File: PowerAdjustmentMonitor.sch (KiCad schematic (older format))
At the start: 18 parts, among them U5002 LM324, U6001 LM317, U6002 LM317, U6003 7805, U6004 7805

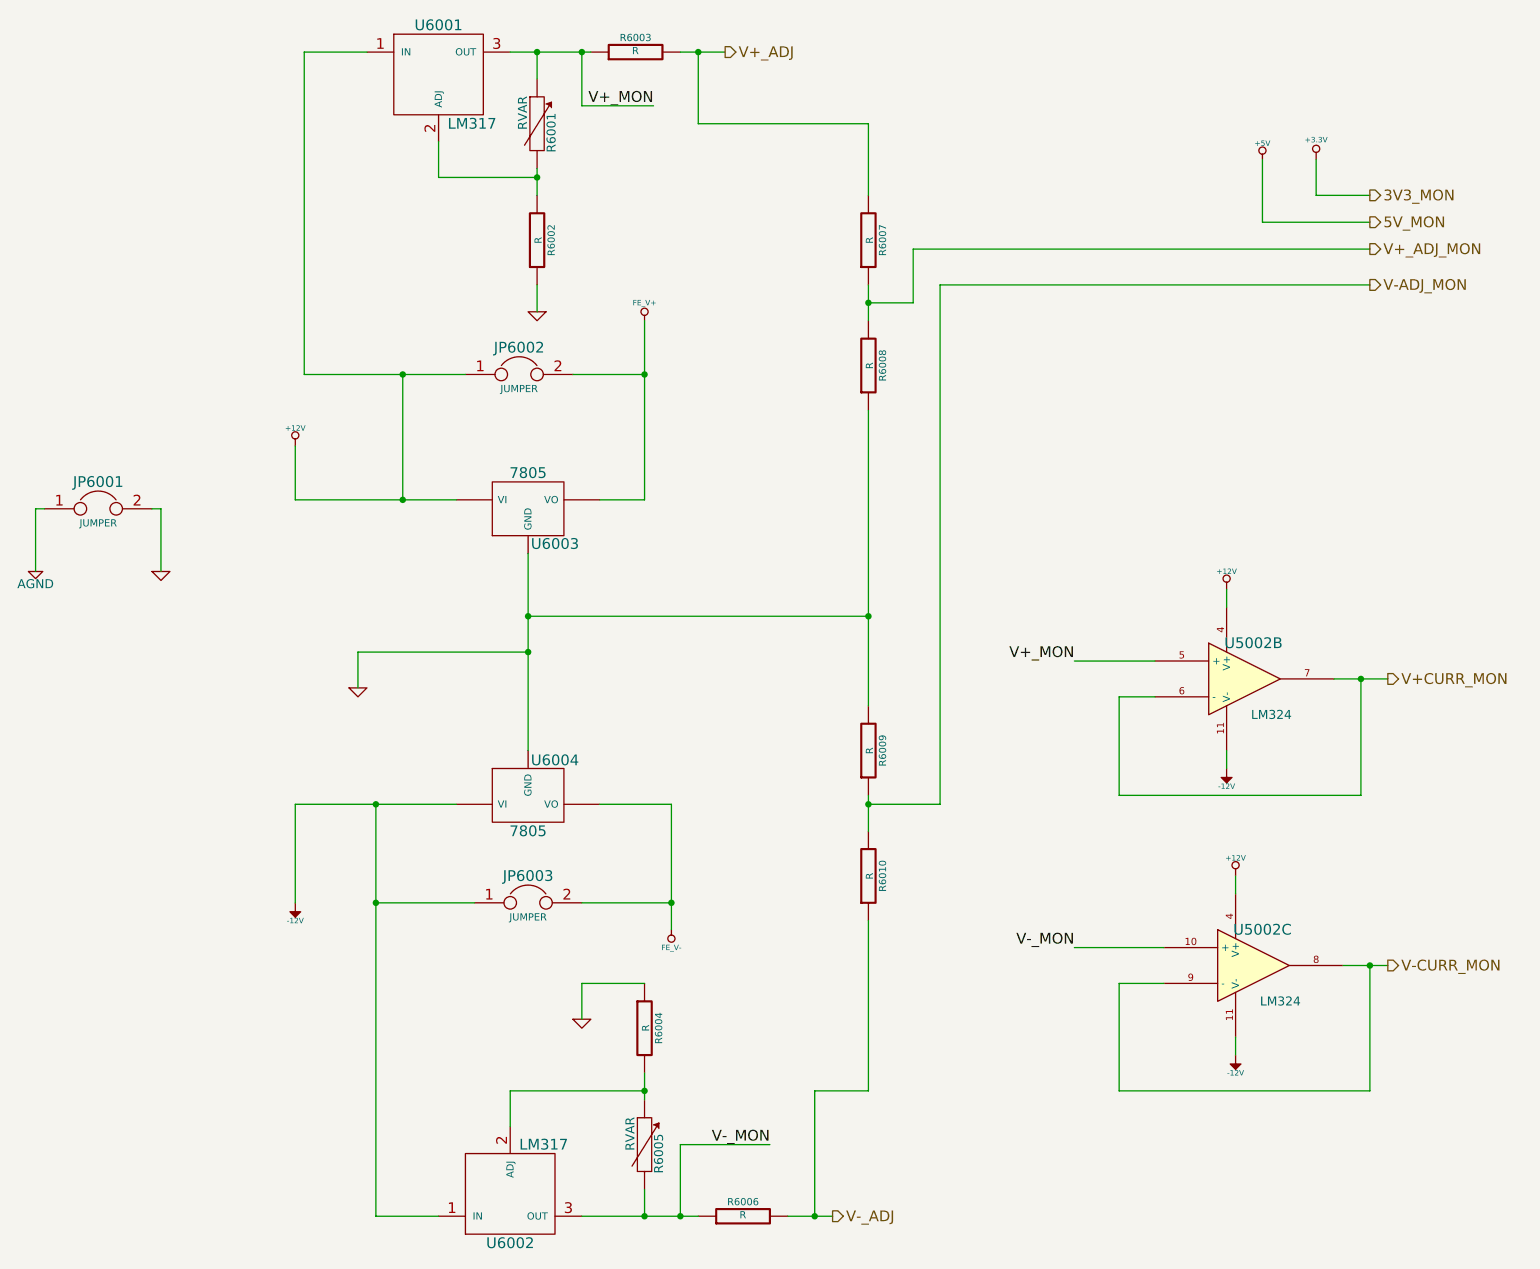
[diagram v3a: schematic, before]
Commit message: Added Arduino Connect Pin Layout
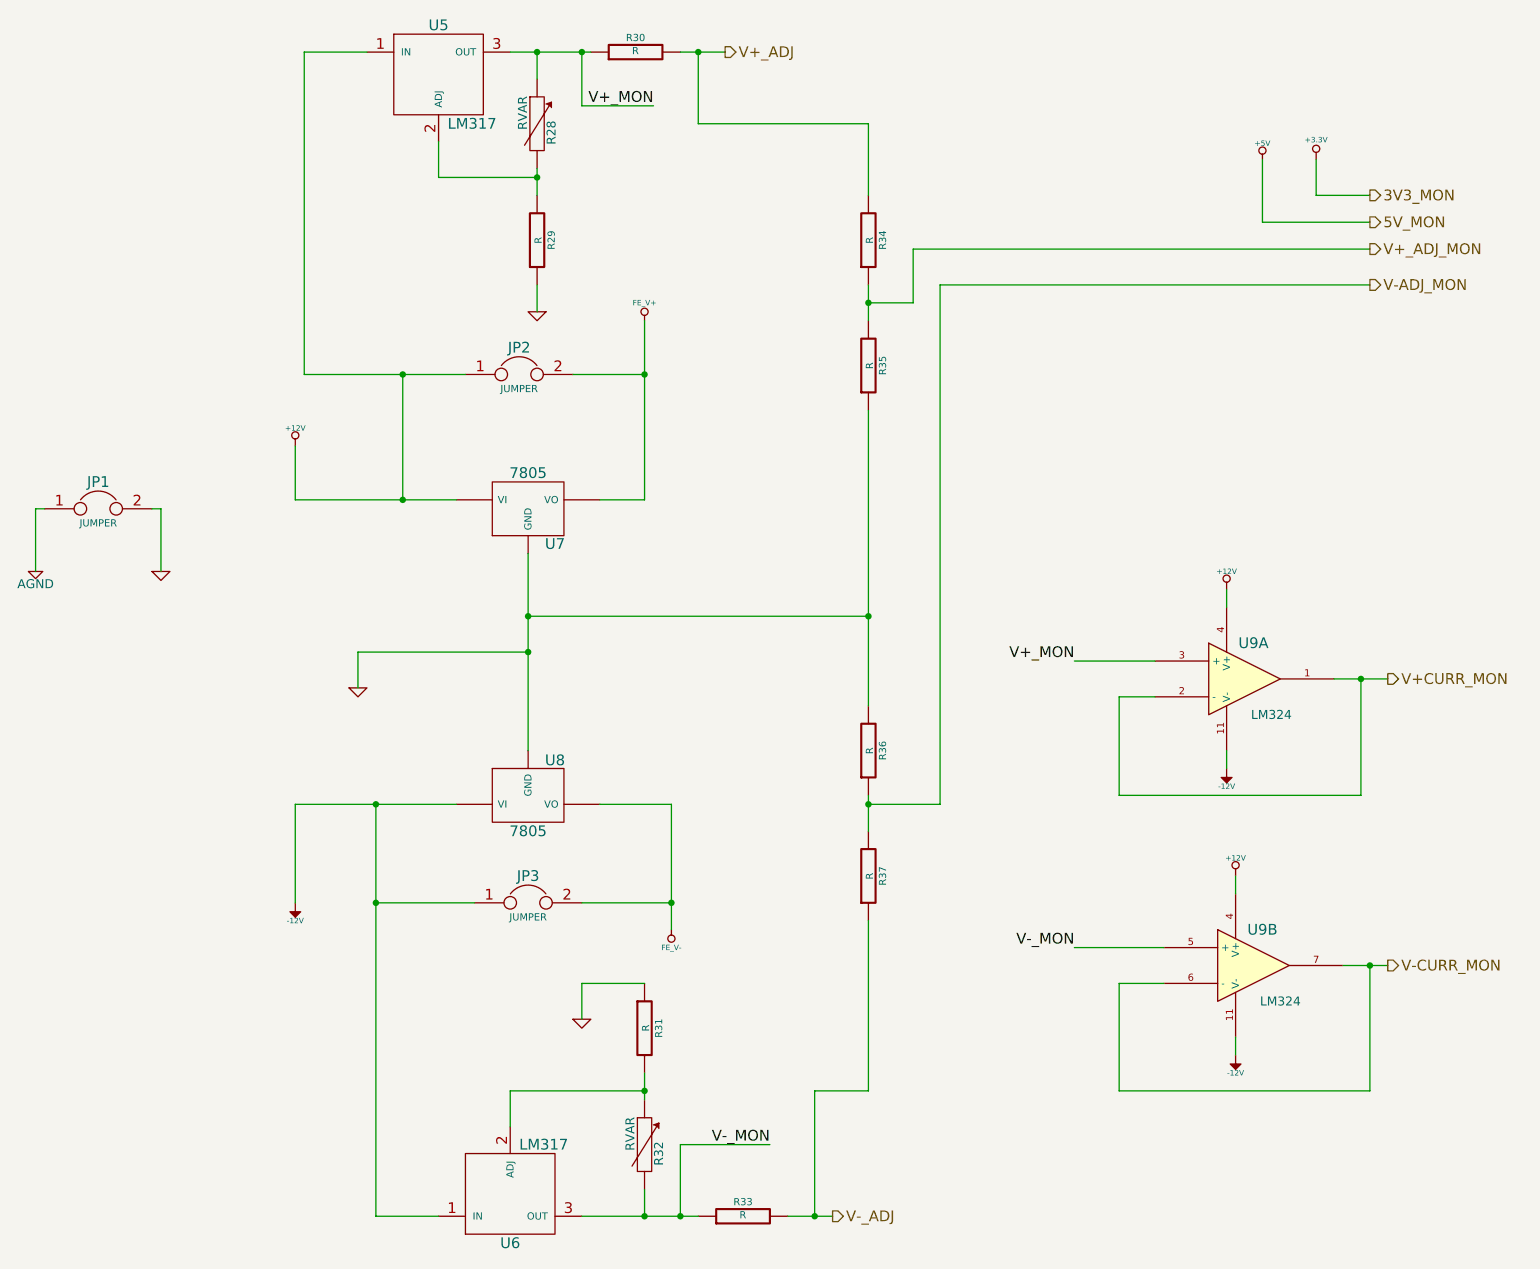
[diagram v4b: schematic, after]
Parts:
- renumbered JP6001 to JP1, JP6002 to JP2, JP6003 to JP3, R6001 to R28, R6002 to R29, R6003 to R30, R6004 to R31, R6005 to R32, R6006 to R33, R6007 to R34, R6008 to R35, R6009 to R36, R6010 to R37, U6001 to U5, U6002 to U6, U6003 to U7, U6004 to U8, U5002 to U9
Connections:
- net V+CURR_MON: now also U9.1, U9.2 (-); no longer U9.6 (-), U9.7
- net V+_MON: now also U9.3 (+); no longer U9.5 (+)
- net V-CURR_MON: now also U9.6 (-), U9.7; no longer U9.8, U9.9 (-)
- net V-_MON: now also U9.5 (+); no longer U9.10 (+)
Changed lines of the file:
@@
 $EndDescr
 $Comp
-L +3.3V #PWR6015
+L +3.3V #PWR39
 U 1 1 52F258C0
 P 9300 1600
-F 0 "#PWR6015" H 9300 1560 30  0001 C CNN
+F 0 "#PWR39" H 9300 1560 30  0001 C CNN
 F 1 "+3.3V" H 9300 1710 30  0000 C CNN
 F 2 "" H 9300 1600 60  0000 C CNN
@@
 $EndComp
 $Comp
-L +5V #PWR6014
+L +5V #PWR38
 U 1 1 52F258C6
 P 9000 1600
-F 0 "#PWR6014" H 9000 1690 20  0001 C CNN
+F 0 "#PWR38" H 9000 1690 20  0001 C CNN
 F 1 "+5V" H 9000 1690 30  0000 C CNN
 F 2 "" H 9000 1600 60  0000 C CNN
@@
 $EndComp
 $Comp
-L GND #PWR6005
+L GND #PWR29
 U 1 1 52F2592B
 P 3950 4550
-F 0 "#PWR6005" H 3950 4550 30  0001 C CNN
+F 0 "#PWR29" H 3950 4550 30  0001 C CNN
 F 1 "GND" H 3950 4480 30  0001 C CNN
 F 2 "" H 3950 4550 60  0000 C CNN
@@
 $EndComp
 $Comp
-L -12V #PWR6004
+L -12V #PWR28
 U 1 1 52F25955
 P 3600 5750
-F 0 "#PWR6004" H 3600 5880 20  0001 C CNN
+F 0 "#PWR28" H 3600 5880 20  0001 C CNN
 F 1 "-12V" H 3600 5850 30  0000 C CNN
 F 2 "" H 3600 5750 60  0000 C CNN
@@
 $EndComp
 $Comp
-L +12V #PWR6003
+L +12V #PWR27
 U 1 1 52F25965
 P 3600 3200
-F 0 "#PWR6003" H 3600 3150 20  0001 C CNN
+F 0 "#PWR27" H 3600 3150 20  0001 C CNN
 F 1 "+12V" H 3600 3300 30  0000 C CNN
 F 2 "" H 3600 3200 60  0000 C CNN
@@
 $EndComp
 $Comp
-L LM317 U6002
+L LM317 U6
 U 1 1 52F25974
 P 4800 7350
-F 0 "U6002" H 4800 7650 60  0000 C CNN
+F 0 "U6" H 4800 7650 60  0000 C CNN
 F 1 "LM317" H 4850 7100 60  0000 L CNN
 F 2 "~" H 4800 7350 60  0000 C CNN
@@
 $EndComp
 $Comp
-L JUMPER JP6002
+L JUMPER JP2
 U 1 1 52F259A2
 P 4850 2800
-F 0 "JP6002" H 4850 2950 60  0000 C CNN
+F 0 "JP2" H 4850 2950 60  0000 C CNN
 F 1 "JUMPER" H 4850 2720 40  0000 C CNN
 F 2 "~" H 4850 2800 60  0000 C CNN
@@
 $EndComp
 $Comp
-L JUMPER JP6003
+L JUMPER JP3
 U 1 1 52F259AF
 P 4900 5750
-F 0 "JP6003" H 4900 5900 60  0000 C CNN
+F 0 "JP3" H 4900 5900 60  0000 C CNN
 F 1 "JUMPER" H 4900 5670 40  0000 C CNN
 F 2 "~" H 4900 5750 60  0000 C CNN
@@
 $EndComp
 $Comp
-L AGND #PWR6001
+L AGND #PWR25
 U 1 1 52F25DEE
 P 2150 3900
-F 0 "#PWR6001" H 2150 3900 40  0001 C CNN
+F 0 "#PWR25" H 2150 3900 40  0001 C CNN
 F 1 "AGND" H 2150 3830 50  0000 C CNN
 F 2 "" H 2150 3900 60  0000 C CNN
@@
 $EndComp
 $Comp
-L JUMPER JP6001
+L JUMPER JP1
 U 1 1 52F25DFB
 P 2500 3550
-F 0 "JP6001" H 2500 3700 60  0000 C CNN
+F 0 "JP1" H 2500 3700 60  0000 C CNN
 F 1 "JUMPER" H 2500 3470 40  0000 C CNN
 F 2 "~" H 2500 3550 60  0000 C CNN
@@
 $EndComp
 $Comp
-L GND #PWR6002
+L GND #PWR26
 U 1 1 52F25E16
 P 2850 3900
-F 0 "#PWR6002" H 2850 3900 30  0001 C CNN
+F 0 "#PWR26" H 2850 3900 30  0001 C CNN
 F 1 "GND" H 2850 3830 30  0001 C CNN
 F 2 "" H 2850 3900 60  0000 C CNN
@@
 $EndComp
 $Comp
-L FE_V+ #PWR6008
+L FE_V+ #PWR32
 U 1 1 52F25E8D
 P 5550 2500
-F 0 "#PWR6008" H 5550 2600 30  0001 C CNN
+F 0 "#PWR32" H 5550 2600 30  0001 C CNN
 F 1 "FE_V+" H 5550 2600 30  0000 C CNN
 F 2 "" H 5550 2500 60  0000 C CNN
@@
 $EndComp
 $Comp
-L FE_V- #PWR6009
+L FE_V- #PWR33
 U 1 1 52F25E9C
 P 5700 5900
-F 0 "#PWR6009" H 5700 6000 30  0001 C CNN
+F 0 "#PWR33" H 5700 6000 30  0001 C CNN
 F 1 "FE_V-" H 5700 6000 30  0000 C CNN
 F 2 "" H 5700 5900 60  0000 C CNN
@@
 $EndComp
 $Comp
-L 7805 U6003
+L 7805 U7
 U 1 1 52F25F16
 P 4900 3550
-F 0 "U6003" H 5050 3354 60  0000 C CNN
+F 0 "U7" H 5050 3354 60  0000 C CNN
 F 1 "7805" H 4900 3750 60  0000 C CNN
 F 2 "~" H 4900 3550 60  0000 C CNN
@@
 $EndComp
 $Comp
-L 7805 U6004
+L 7805 U8
 U 1 1 52F25F23
 P 4900 5150
-F 0 "U6004" H 5050 4954 60  0000 C CNN
+F 0 "U8" H 5050 4954 60  0000 C CNN
 F 1 "7805" H 4900 5350 60  0000 C CNN
 F 2 "~" H 4900 5150 60  0000 C CNN
@@
 $EndComp
 $Comp
-L R R6004
+L R R31
 U 1 1 52F25FD8
 P 5550 6450
-F 0 "R6004" V 5630 6450 40  0000 C CNN
+F 0 "R31" V 5630 6450 40  0000 C CNN
 F 1 "R" V 5557 6451 40  0000 C CNN
 F 2 "~" V 5480 6450 30  0000 C CNN
@@
 $EndComp
 $Comp
-L GND #PWR6007
+L GND #PWR31
 U 1 1 52F26054
 P 5200 6400
-F 0 "#PWR6007" H 5200 6400 30  0001 C CNN
+F 0 "#PWR31" H 5200 6400 30  0001 C CNN
 F 1 "GND" H 5200 6330 30  0001 C CNN
 F 2 "" H 5200 6400 60  0000 C CNN
@@
 $EndComp
 $Comp
-L LM317 U6001
+L LM317 U5
 U 1 1 52F26114
 P 4400 1150
-F 0 "U6001" H 4400 1450 60  0000 C CNN
+F 0 "U5" H 4400 1450 60  0000 C CNN
 F 1 "LM317" H 4450 900 60  0000 L CNN
 F 2 "~" H 4400 1150 60  0000 C CNN
@@
 $EndComp
 $Comp
-L R R6002
+L R R29
 U 1 1 52F26120
 P 4950 2050
-F 0 "R6002" V 5030 2050 40  0000 C CNN
+F 0 "R29" V 5030 2050 40  0000 C CNN
 F 1 "R" V 4957 2051 40  0000 C CNN
 F 2 "~" V 4880 2050 30  0000 C CNN
@@
 $EndComp
 $Comp
-L GND #PWR6006
+L GND #PWR30
 U 1 1 52F2612C
 P 4950 2450
-F 0 "#PWR6006" H 4950 2450 30  0001 C CNN
+F 0 "#PWR30" H 4950 2450 30  0001 C CNN
 F 1 "GND" H 4950 2380 30  0001 C CNN
 F 2 "" H 4950 2450 60  0000 C CNN
@@
 V-CURR_MON
 $Comp
-L R R6007
+L R R34
 U 1 1 52F261D2
 P 6800 2050
-F 0 "R6007" V 6880 2050 40  0000 C CNN
+F 0 "R34" V 6880 2050 40  0000 C CNN
 F 1 "R" V 6807 2051 40  0000 C CNN
 F 2 "~" V 6730 2050 30  0000 C CNN
@@
 $EndComp
 $Comp
-L R R6008
+L R R35
 U 1 1 52F261D8
 P 6800 2750
-F 0 "R6008" V 6880 2750 40  0000 C CNN
+F 0 "R35" V 6880 2750 40  0000 C CNN
 F 1 "R" V 6807 2751 40  0000 C CNN
 F 2 "~" V 6730 2750 30  0000 C CNN
@@
 $EndComp
 $Comp
-L R R6009
+L R R36
 U 1 1 52F261DE
 P 6800 4900
-F 0 "R6009" V 6880 4900 40  0000 C CNN
+F 0 "R36" V 6880 4900 40  0000 C CNN
 F 1 "R" V 6807 4901 40  0000 C CNN
 F 2 "~" V 6730 4900 30  0000 C CNN
@@
 $EndComp
 $Comp
-L R R6010
+L R R37
 U 1 1 52F261E4
 P 6800 5600
-F 0 "R6010" V 6880 5600 40  0000 C CNN
+F 0 "R37" V 6880 5600 40  0000 C CNN
 F 1 "R" V 6807 5601 40  0000 C CNN
 F 2 "~" V 6730 5600 30  0000 C CNN
@@
 	9000 1950 9600 1950
 $Comp
-L R R6006
+L R R33
 U 1 1 52F2653F
 P 6100 7500
-F 0 "R6006" V 6180 7500 40  0000 C CNN
+F 0 "R33" V 6180 7500 40  0000 C CNN
 F 1 "R" V 6107 7501 40  0000 C CNN
 F 2 "~" V 6030 7500 30  0000 C CNN
@@
 	6350 7500 6600 7500
 $Comp
-L R R6003
+L R R30
 U 1 1 52F26669
 P 5500 1000
-F 0 "R6003" V 5580 1000 40  0000 C CNN
+F 0 "R30" V 5580 1000 40  0000 C CNN
 F 1 "R" V 5507 1001 40  0000 C CNN
 F 2 "~" V 5430 1000 30  0000 C CNN
@@
 Connection ~ 4950 1000
 $Comp
-L LM324 U5002
-U 3 1 52F26EAF
+L LM324 U9
+U 2 1 52F26EAF
 P 8950 6100
-F 0 "U5002" H 9000 6300 60  0000 C CNN
+F 0 "U9" H 9000 6300 60  0000 C CNN
 F 1 "LM324" H 9100 5900 50  0000 C CNN
 F 2 "" H 8950 6100 60  0000 C CNN
 F 3 "" H 8950 6100 60  0000 C CNN
-	3    8950 6100
-	1    0    0    -1
-$EndComp
-$Comp
-L -12V #PWR6013
+	2    8950 6100
+	1    0    0    -1
+$EndComp
+$Comp
+L -12V #PWR37
 U 1 1 52F26EBC
 P 8850 6600
-F 0 "#PWR6013" H 8850 6730 20  0001 C CNN
+F 0 "#PWR37" H 8850 6730 20  0001 C CNN
 F 1 "-12V" H 8850 6700 30  0000 C CNN
 F 2 "" H 8850 6600 60  0000 C CNN
@@
 $EndComp
 $Comp
-L +12V #PWR6012
+L +12V #PWR36
 U 1 1 52F26EC2
 P 8850 5600
-F 0 "#PWR6012" H 8850 5550 20  0001 C CNN
+F 0 "#PWR36" H 8850 5550 20  0001 C CNN
 F 1 "+12V" H 8850 5700 30  0000 C CNN
 F 2 "" H 8850 5600 60  0000 C CNN
@@
 	8850 6600 8850 6500
 $Comp
-L LM324 U5002
-U 2 1 52F27003
+L LM324 U9
+U 1 1 52F27003
 P 8900 4500
-F 0 "U5002" H 8950 4700 60  0000 C CNN
+F 0 "U9" H 8950 4700 60  0000 C CNN
 F 1 "LM324" H 9050 4300 50  0000 C CNN
 F 2 "" H 8900 4500 60  0000 C CNN
 F 3 "" H 8900 4500 60  0000 C CNN
-	2    8900 4500
-	1    0    0    -1
-$EndComp
-$Comp
-L -12V #PWR6011
+	1    8900 4500
+	1    0    0    -1
+$EndComp
+$Comp
+L -12V #PWR35
 U 1 1 52F27009
 P 8800 5000
-F 0 "#PWR6011" H 8800 5130 20  0001 C CNN
+F 0 "#PWR35" H 8800 5130 20  0001 C CNN
 F 1 "-12V" H 8800 5100 30  0000 C CNN
 F 2 "" H 8800 5000 60  0000 C CNN
@@
 $EndComp
 $Comp
-L +12V #PWR6010
+L +12V #PWR34
 U 1 1 52F2700F
 P 8800 4000
-F 0 "#PWR6010" H 8800 3950 20  0001 C CNN
+F 0 "#PWR34" H 8800 3950 20  0001 C CNN
 F 1 "+12V" H 8800 4100 30  0000 C CNN
 F 2 "" H 8800 4000 60  0000 C CNN
@@
 V-_MON
 $Comp
-L RVAR R6005
+L RVAR R32
 U 1 1 52F275AF
 P 5550 7100
-F 0 "R6005" V 5630 7050 50  0000 C CNN
+F 0 "R32" V 5630 7050 50  0000 C CNN
 F 1 "RVAR" V 5470 7160 50  0000 C CNN
 F 2 "~" H 5550 7100 60  0000 C CNN
@@
 $EndComp
 $Comp
-L RVAR R6001
+L RVAR R28
 U 1 1 52F275BE
 P 4950 1400
-F 0 "R6001" V 5030 1350 50  0000 C CNN
+F 0 "R28" V 5030 1350 50  0000 C CNN
 F 1 "RVAR" V 4870 1460 50  0000 C CNN
 F 2 "~" H 4950 1400 60  0000 C CNN
